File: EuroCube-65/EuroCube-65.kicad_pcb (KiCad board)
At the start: 2 copper layers, 160 x 100 mm, 105 parts, among them CON1 SERIAL PORT, CON2 PARALLEL PORT, CON3 EXPANSION BUS, IC1 6551A, IC10 GAL16V8, IC11 6522, IC12 6502, IC13 7660, IC2 26LS30, IC3 M3002, IC4 26LS32, IC5 74LS04, IC7 74LS00, IC8 74HCT132, IC9 GAL16V8, T1 BC547, T2 2N7000, T3 2N3906, X1 1.843MHz, X2 32.768kHz, X3 1MHz

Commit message: All laid out, ready to route
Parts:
- removed REF**: DIN41612_B_2x32_Male_Horizontal_THT, Connector_DIN:DIN41612_B_2x32_Male_Horizontal_THT
- moved R31 287.2 mm to (67.0, 81.6)
- moved X1 282.4 mm to (93.8, 56.5), turned to 90 degrees
- moved L3 253.8 mm to (95.2, 80.3)
- moved L2 252.9 mm to (92.4, 80.3)
- moved B1 251.0 mm to (121.9, 56.4), turned to 180 degrees
- moved L4 247.6 mm to (109.7, 69.9), turned to 90 degrees
- moved R14 247.3 mm to (92.9, 92.7)
- moved TP1 247.2 mm to (70.6, 55.4)
- moved R13 247.2 mm to (92.9, 89.7)
- moved R15 245.3 mm to (98.3, 70.9)
- moved R30 244.9 mm to (109.0, 83.8), turned to -90 degrees
- moved R29 244.7 mm to (109.0, 80.8), turned to 90 degrees
- moved R11 243.4 mm to (92.9, 77.5)
- moved R9 243.4 mm to (92.7, 71.2), turned to 90 degrees
- moved R10 243.2 mm to (92.9, 74.5)
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
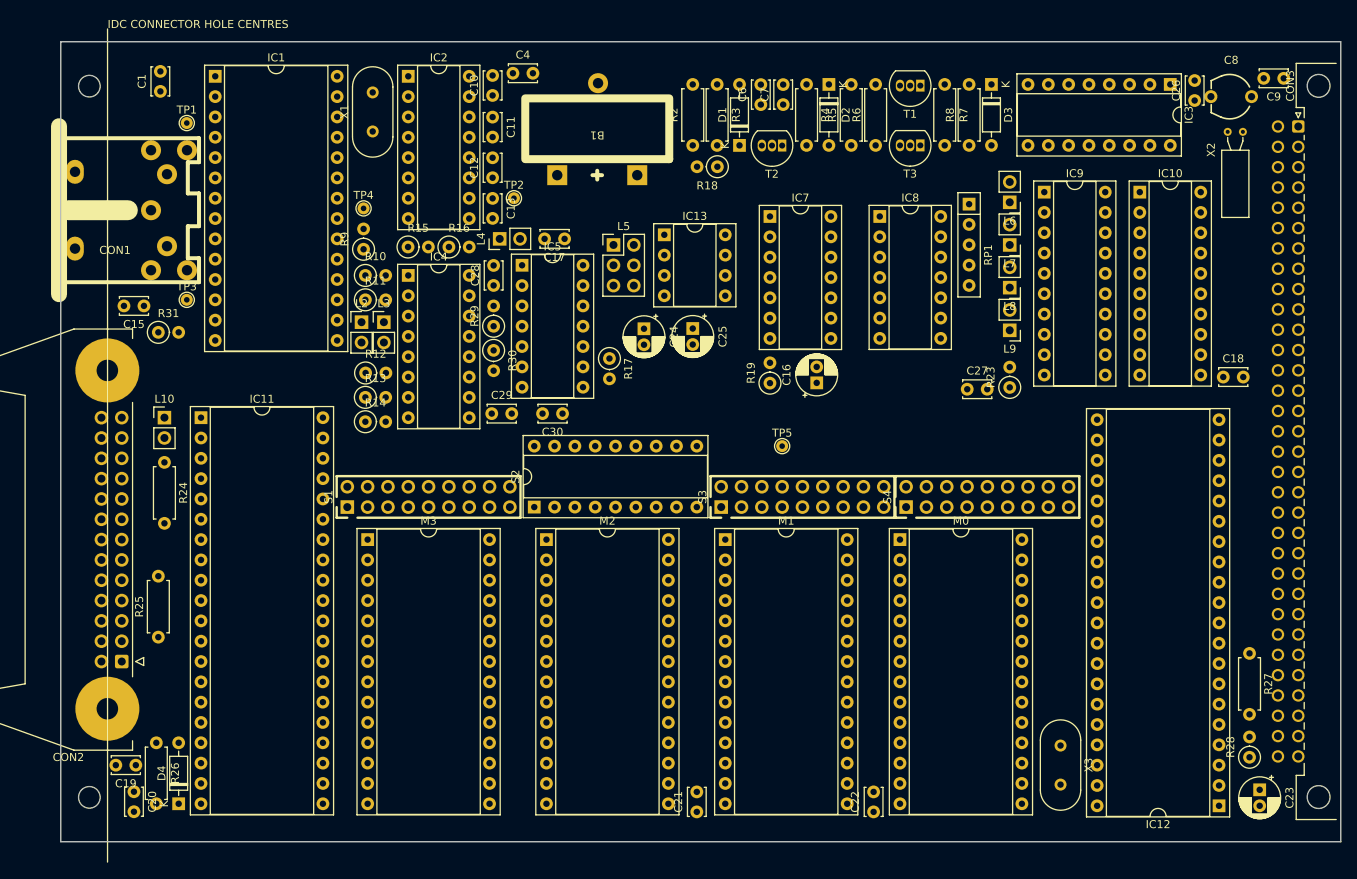
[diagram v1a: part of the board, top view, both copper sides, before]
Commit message: First track layout
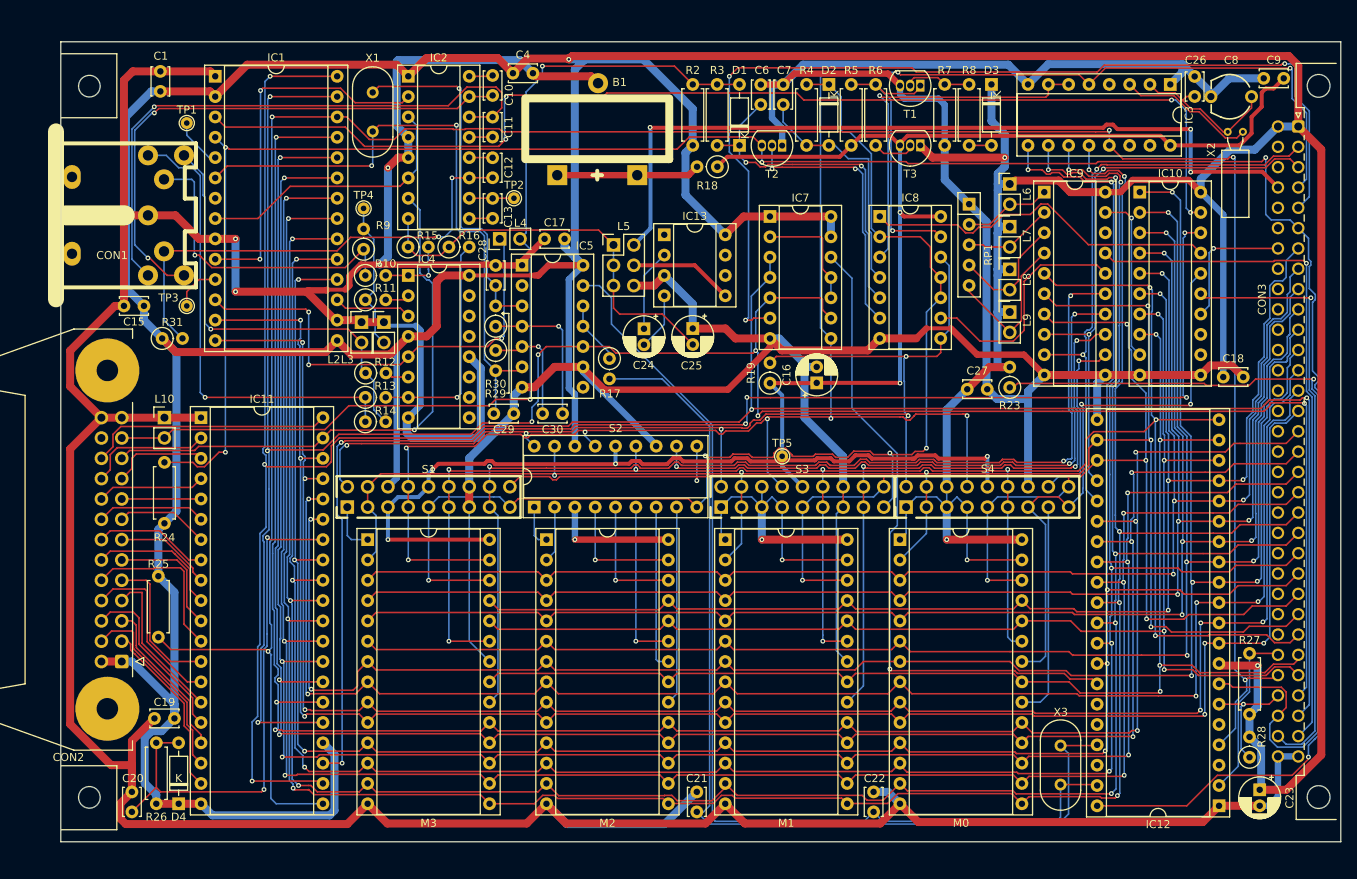
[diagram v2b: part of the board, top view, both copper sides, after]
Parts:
- moved C19 7.58 mm to (69.1, 129.8)
- moved C26 3.01 mm to (196.6, 49.6), turned to -90 degrees
- moved C20 2.53 mm to (63.7, 141.5), turned to 90 degrees
- moved L6 2.29 mm to (173.5, 63.0), turned to 0 degrees
- moved L7 2.29 mm to (173.5, 68.4), turned to 0 degrees
- moved L8 2.29 mm to (173.5, 73.7), turned to 0 degrees
- moved L9 2.29 mm to (173.5, 79.0), turned to 0 degrees
- moved TP5 1.27 mm to (145.0, 97.1)
- moved R31 0.90 mm to (67.5, 82.3)
- moved TP3 0.76 mm to (70.6, 78.3)
- moved CON1 0.75 mm to (56.2, 67.0)
- moved C28 0.25 mm to (109.2, 75.7)
- moved R29 0.25 mm to (109.2, 80.8)
- moved R30 0.25 mm to (109.2, 83.8)
- moved C29 0.25 mm to (109.0, 91.7)
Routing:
- net GND: track 0.00 -> 887.1 mm, vias 0 -> 4
- net +5V: track 0.00 -> 833.5 mm, vias 0 -> 7
- net /~{IRQ}: track 0.00 -> 311.7 mm, vias 0 -> 5
- net D3: track 0.00 -> 302.7 mm, vias 0 -> 8
- net /B_R/~{W}: track 0.00 -> 302.4 mm, vias 0 -> 5
- net D2: track 0.00 -> 301.1 mm, vias 0 -> 8
- net /B_Φ2: track 0.00 -> 298.6 mm, vias 0 -> 8
- net /~{RST}: track 0.00 -> 291.9 mm, vias 0 -> 5
- net D1: track 0.00 -> 291.9 mm, vias 0 -> 8
- net D0: track 0.00 -> 284.5 mm, vias 0 -> 8
- net D7: track 0.00 -> 261.6 mm, vias 0 -> 6
- net D6: track 0.00 -> 255.2 mm, vias 0 -> 6
- net A11: track 0.00 -> 255.1 mm, vias 0 -> 9
- net D5: track 0.00 -> 253.4 mm, vias 0 -> 6
- net D4: track 0.00 -> 251.5 mm, vias 0 -> 6
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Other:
- board text added: "FRONT PANEL"

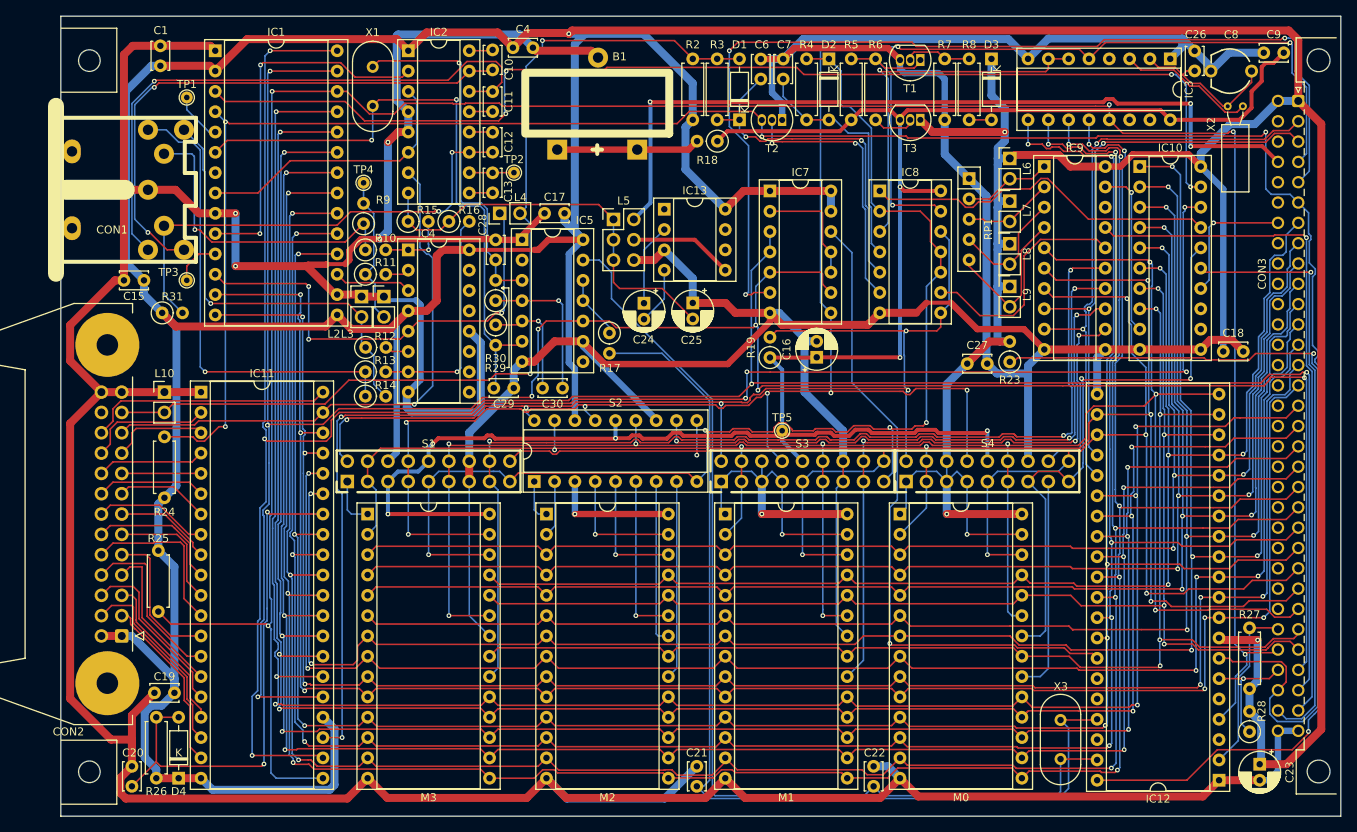
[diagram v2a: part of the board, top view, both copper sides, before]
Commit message: Finished layout
Added coin cell option
Added logo
Added label, issue, contacts to rear
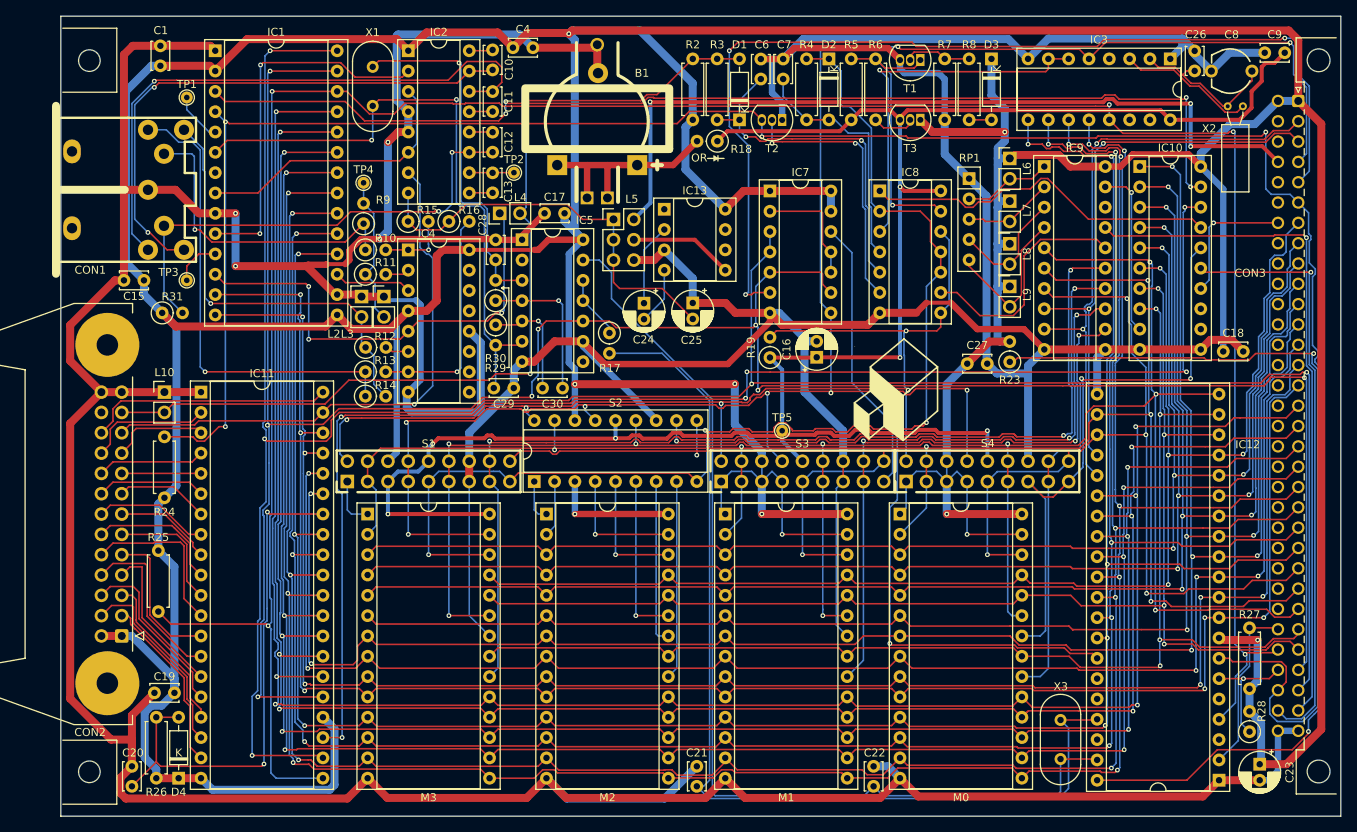
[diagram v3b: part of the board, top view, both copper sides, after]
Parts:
- added G***: LOGO, EuroCube-65:EuroCube-65-logo, F.Cu at (159.2, 92.0)
- moved B1 1.94 mm to (121.9, 58.4)
- moved C9 0.12 mm to (207.8, 49.8)
- moved C8 0.05 mm to (198.7, 54.6)
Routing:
- net +5V: track 833.5 -> 864.3 mm, vias 7 -> 9
- net Net-(B1-+): track 17.9 -> 26.9 mm
- net /~{ACIA}: track 143.8 -> 138.6 mm
- net Net-(CON2-Pin_23): track 122.0 -> 117.2 mm
- net GND: track 887.1 -> 891.8 mm
- net /~{M0}: track 49.9 -> 52.4 mm
- net /~{M0OE}: track 73.3 -> 73.8 mm
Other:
- board text added: "EuroBEEB Single Board Computer Issue 8 steve@croz.co.uk Dec 28 2024"
- board text added: "OR"

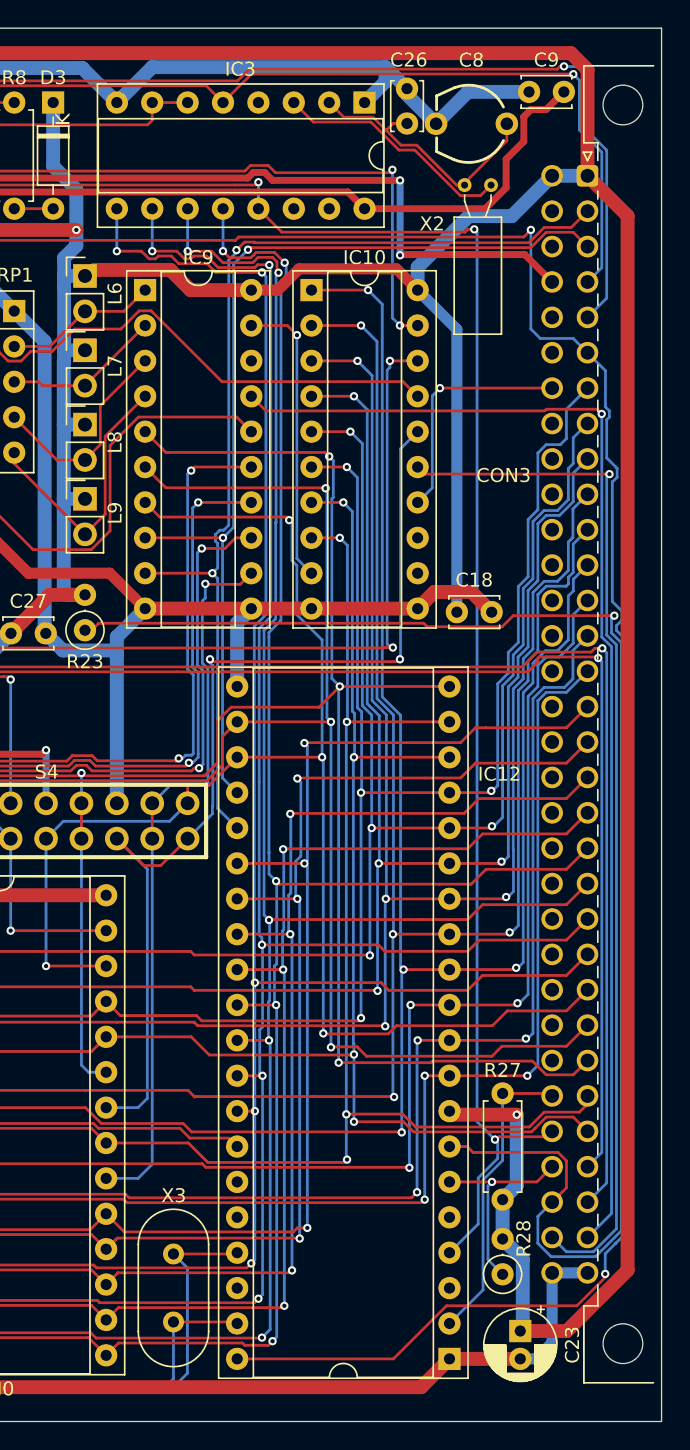
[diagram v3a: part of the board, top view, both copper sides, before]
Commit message: Fixed bus connector location
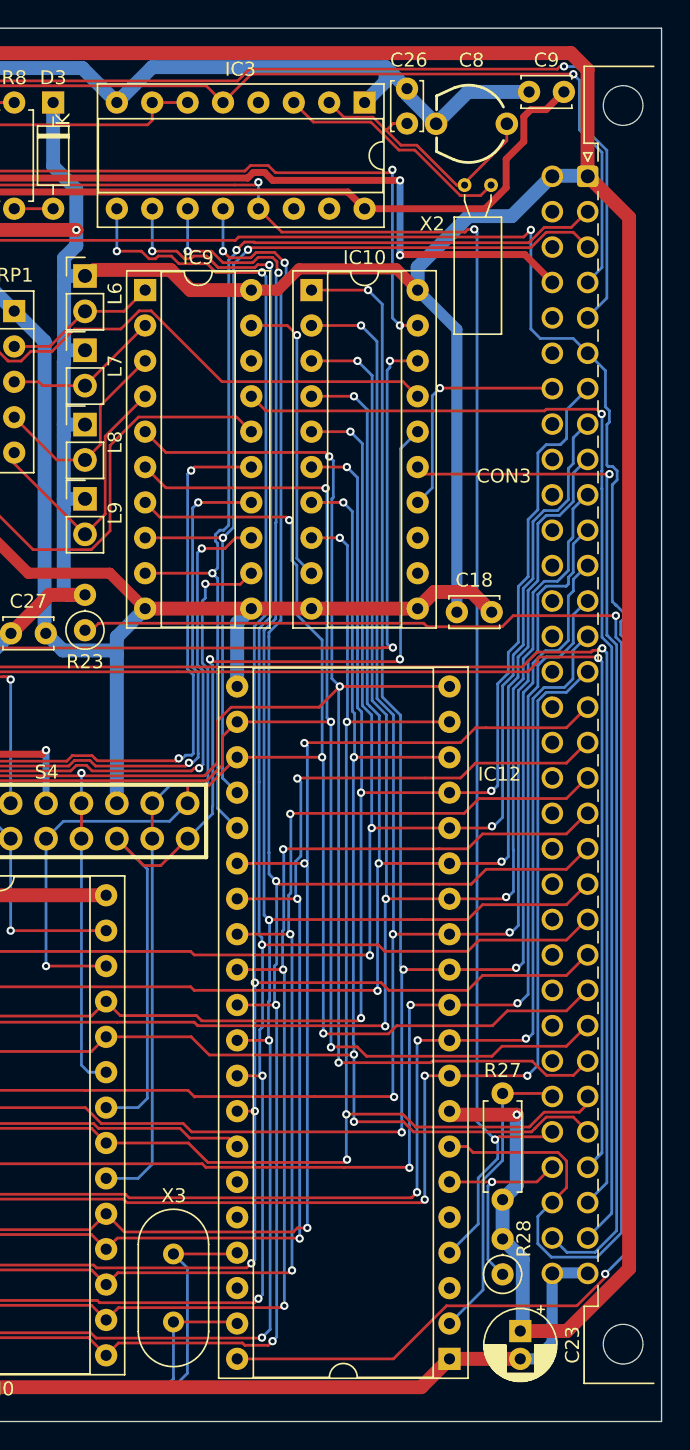
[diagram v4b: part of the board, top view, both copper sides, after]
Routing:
- net /B_Φ2: track 298.6 -> 300.1 mm

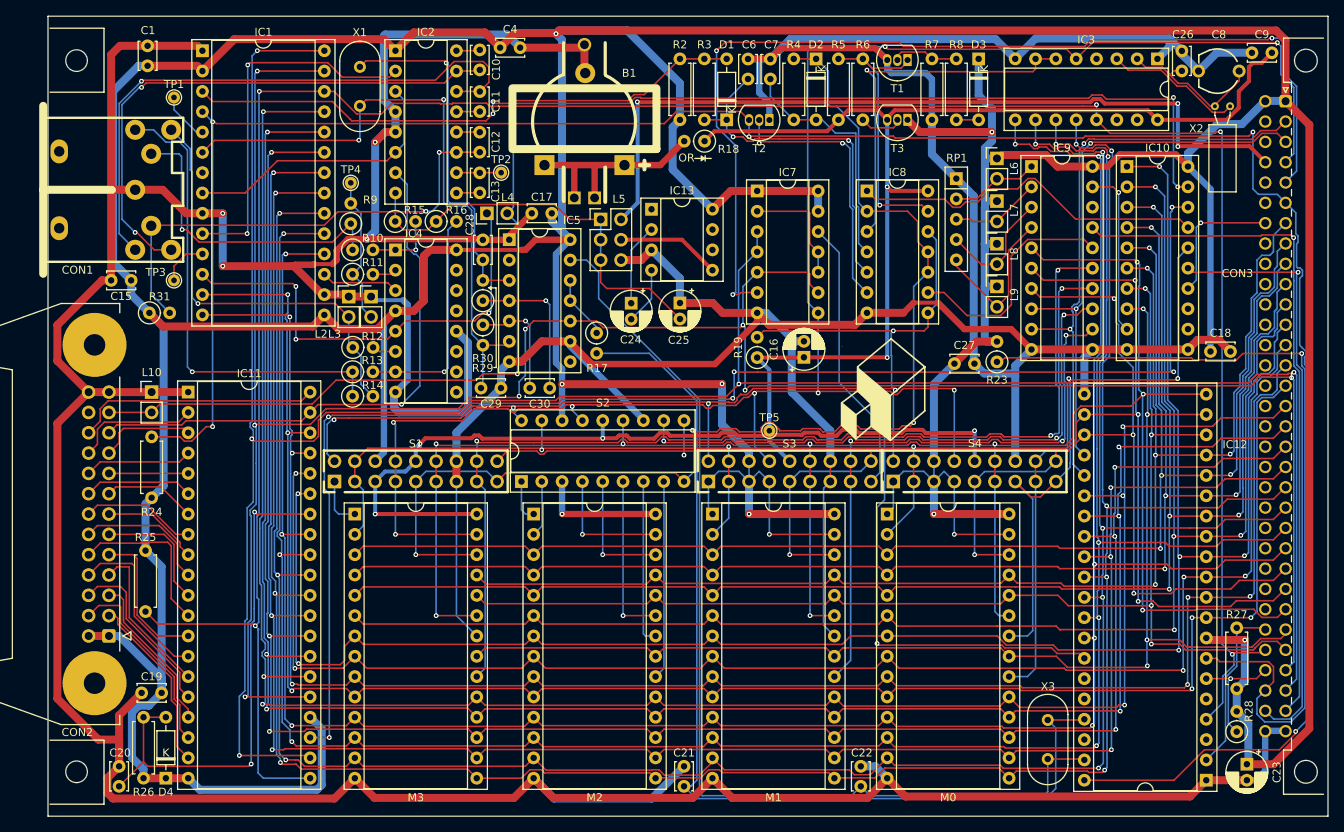
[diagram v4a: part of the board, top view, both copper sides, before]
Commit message: Added filled zones
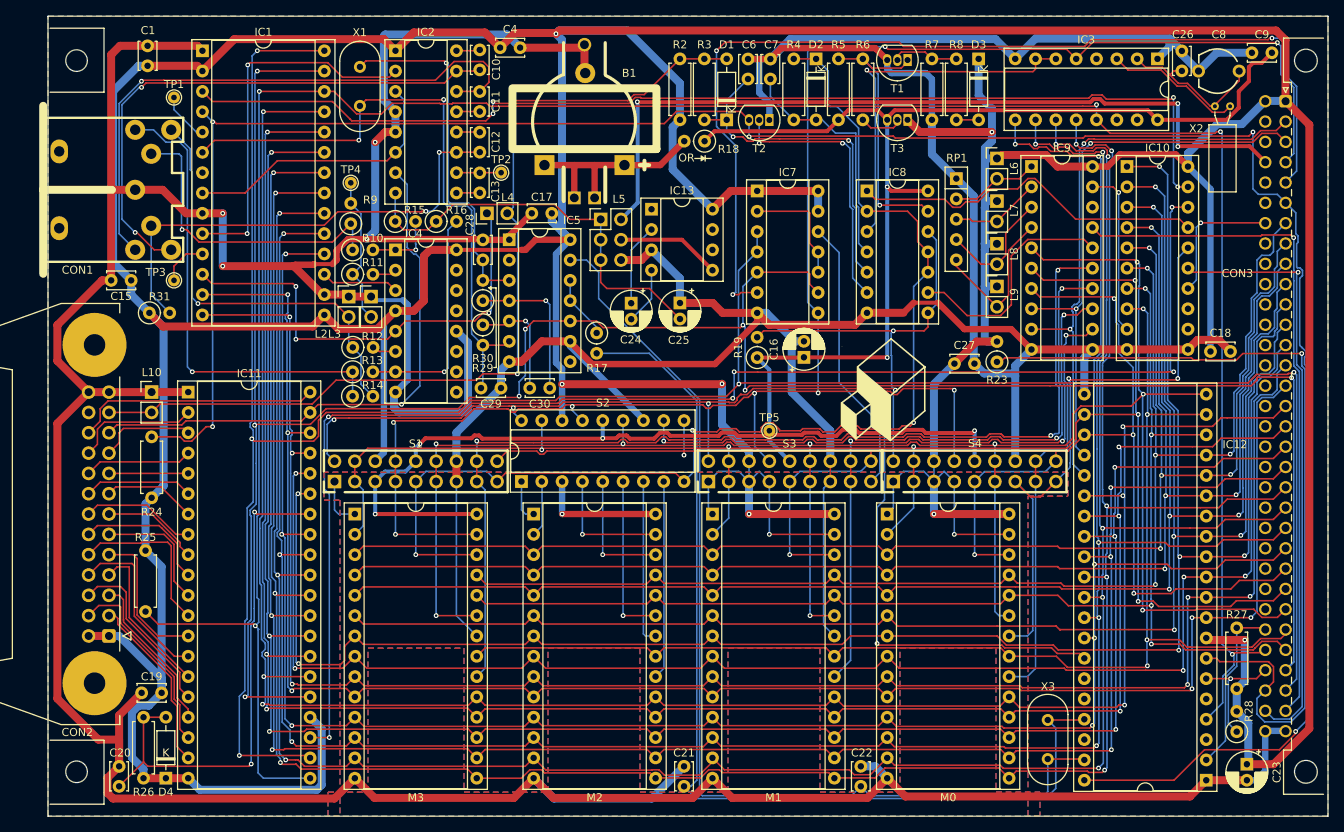
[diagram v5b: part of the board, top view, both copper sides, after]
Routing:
- added copper zone on B.Cu, net GND
- added copper zone on F.Cu, net GND
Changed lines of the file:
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@@
+	)
+	(zone
+		(net 2)
+		(net_name "GND")
+		(layers "F&B.Cu")
+		(hatch edge 0.5)
+		(connect_pads
+			(clearance 0)
+		)
+		(min_thickness 0.25)
+		(filled_areas_thickness no)
+		(fill yes
+			(thermal_gap 0.5)
+			(thermal_bridge_width 0.3)
+		)
+		(polygon
+			(pts
+				(xy 54.85 45.25) (xy 214.85 45.25) (xy 214.85 145.25) (xy 177.35 145.25) (xy 177.35 105.25) (xy 182.35 105.25)
+				(xy 182.35 102.25) (xy 89.35 102.25) (xy 89.35 105.75) (xy 91.35 105.75) (xy 91.35 145.25) (xy 54.85 145.25)
+			)
+		)
+	)
+	(zone
+		(net 2)
+		(net_name "GND")
+		(layers "F&B.Cu")
+		(hatch edge 0.5)
+		(priority 1)
+		(connect_pads
+			(clearance 0)
+		)
+		(min_thickness 0.25)
+		(filled_areas_thickness no)
+		(fill yes
+			(thermal_gap 0.5)
+			(thermal_bridge_width 0.3)
+		)
+		(polygon
+			(pts
+				(xy 94.85 142.25) (xy 94.85 124.25) (xy 106.85 124.25) (xy 106.85 142.25) (xy 117.35 142.25) (xy 117.35 124.25)
+				(xy 128.85 124.25) (xy 128.85 142.25) (xy 139.85 142.25) (xy 139.85 124.25) (xy 151.35 124.25) (xy 151.35 142.25)
+				(xy 161.35 142.25) (xy 161.35 124.25) (xy 173.35 124.25) (xy 173.35 142.25) (xy 178.85 142.25) (xy 178.85 145.25)
+				(xy 89.85 145.25) (xy 89.85 142.25)
+			)
+		)
 	)
 	(zone
